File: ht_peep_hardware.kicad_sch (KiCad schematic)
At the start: 2 parts

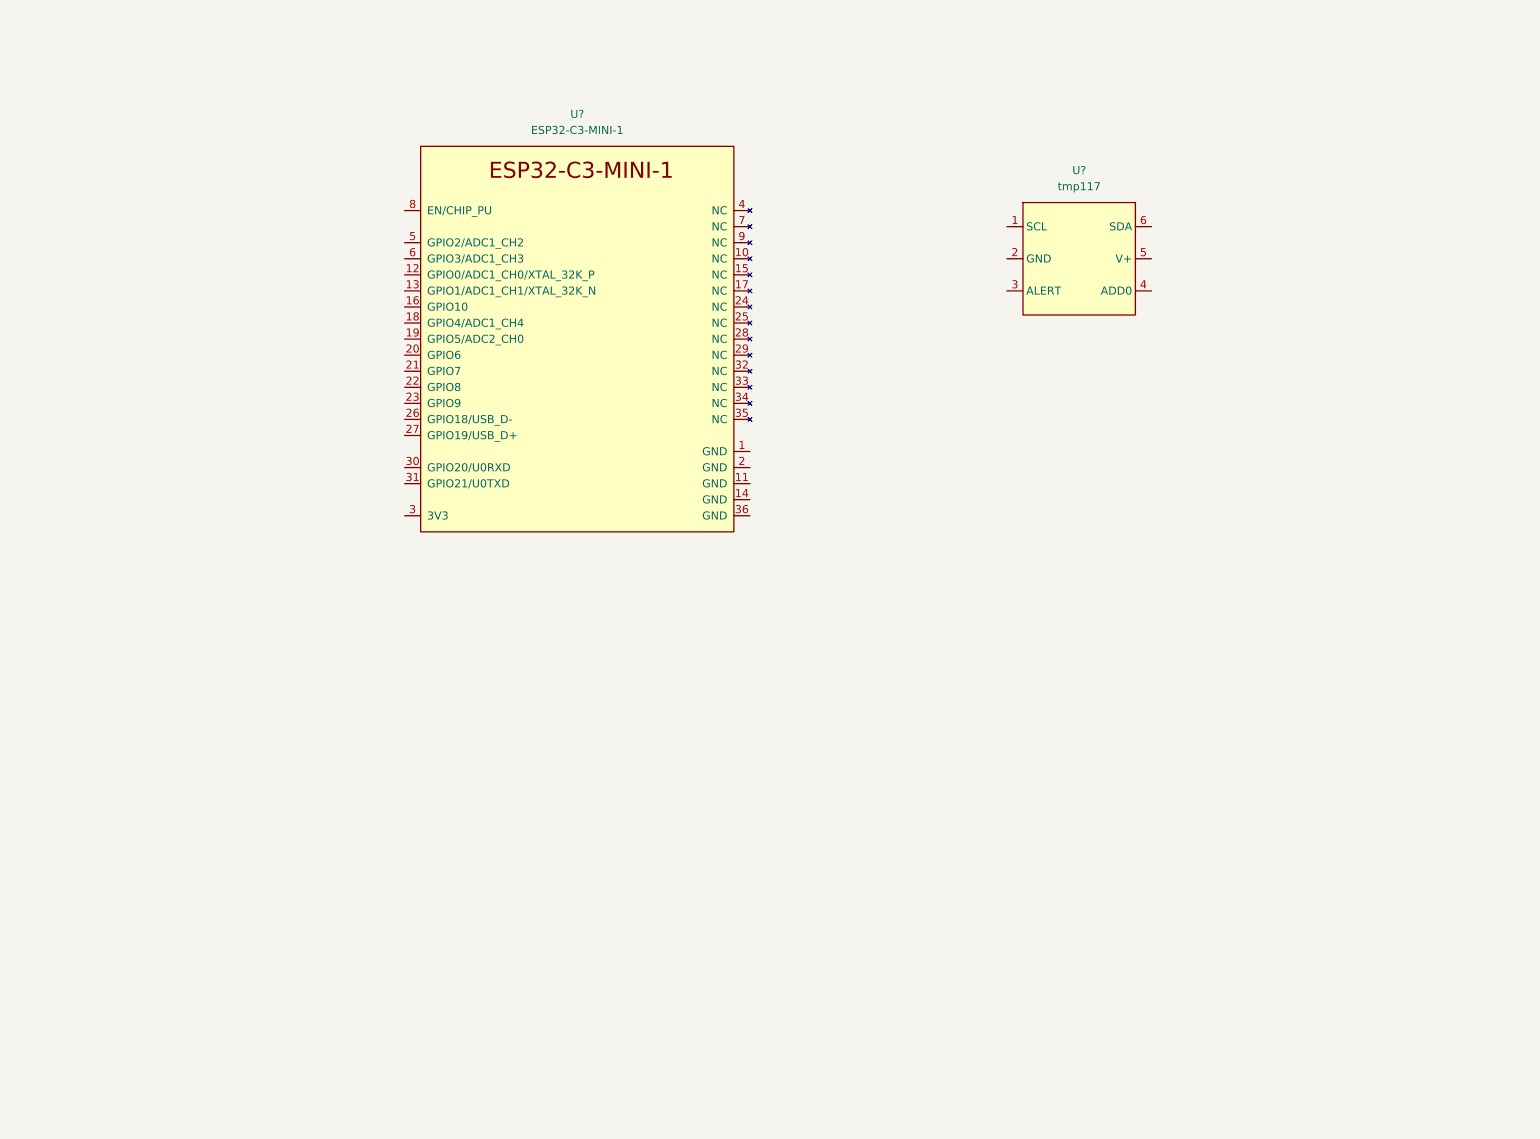
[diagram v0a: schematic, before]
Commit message: updated schematic w/ USB and C1 fix
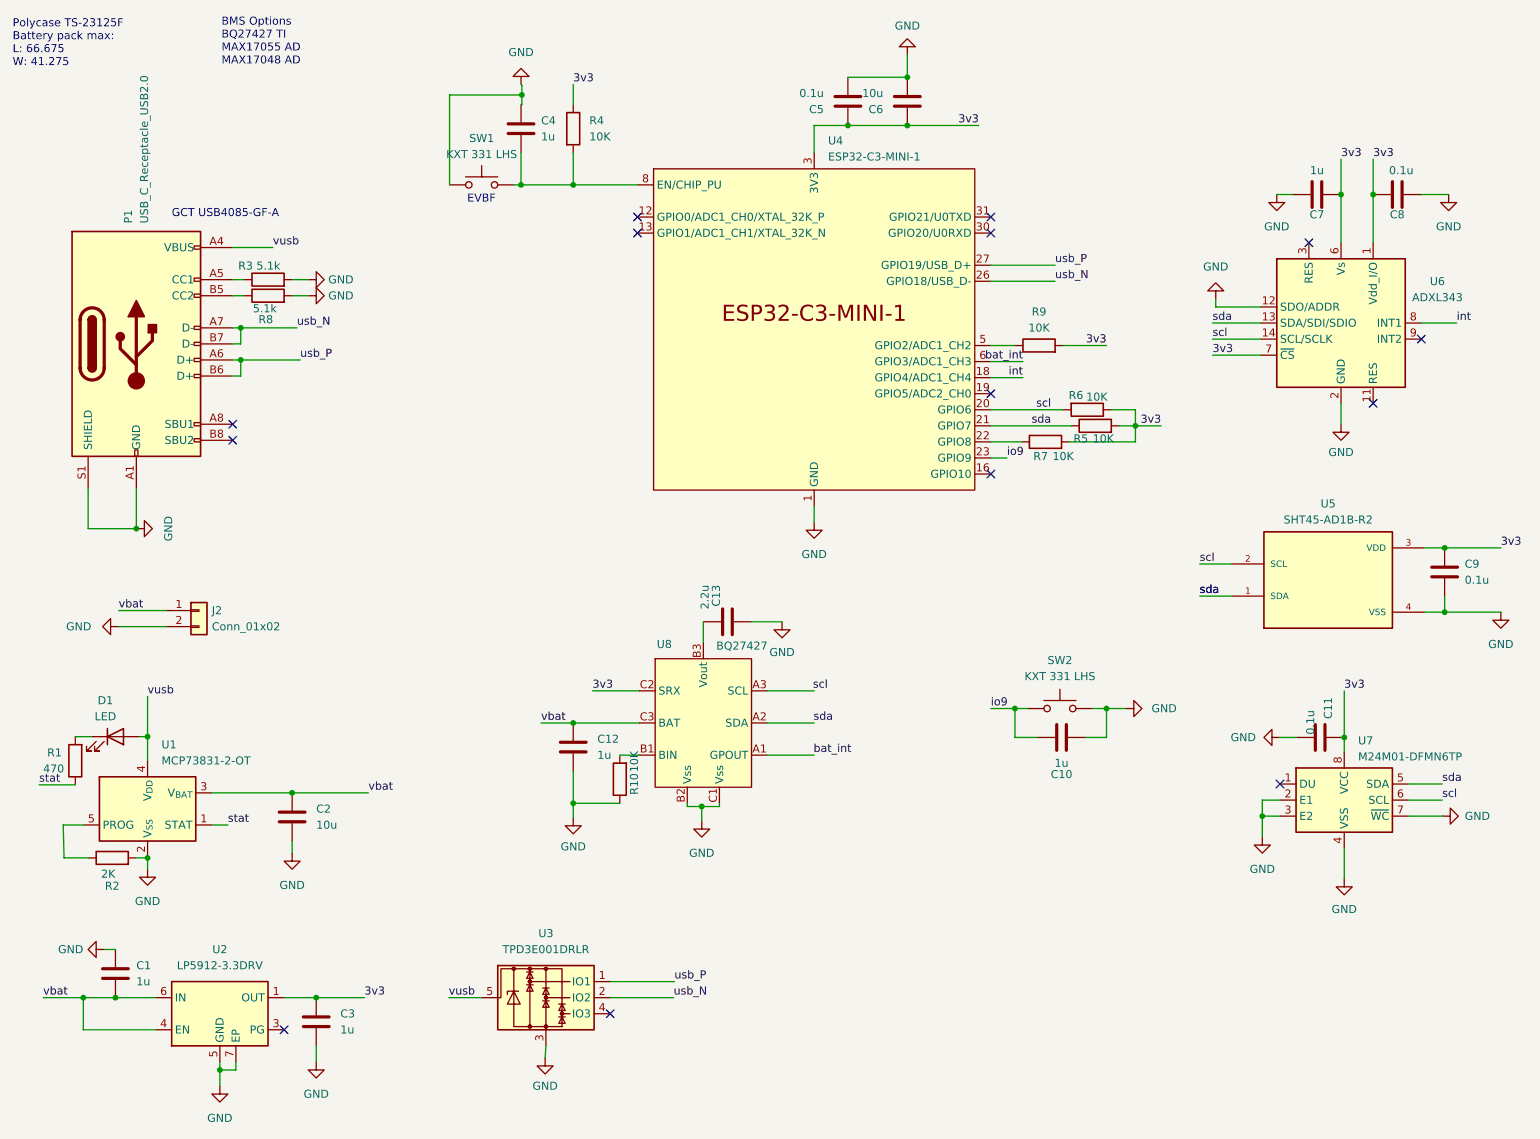
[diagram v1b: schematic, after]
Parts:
- removed U?: ESP32-C3-MINI-1, Espressif:ESP32-C3-MINI-1, symbol Espressif:ESP32-C3-MINI-1
- removed U?: tmp117, Package_SON:WSON-6-1EP_2x2mm_P0.65mm_EP1x1.6mm_ThermalVias, symbol ht_peep_hw:tmp117
- added C1, C10, C12, C3, C4, C7: 1u, Capacitor_SMD:C_0402_1005Metric, symbol Device:C
- added C11, C5, C8, C9: 0.1u, Capacitor_SMD:C_0402_1005Metric, symbol Device:C
- added C13: 2.2u, Capacitor_SMD:C_0402_1005Metric, symbol Device:C
- added C2, C6: 10u, Capacitor_SMD:C_0402_1005Metric, symbol Device:C
- added D1: LED, LED_SMD:LED_0402_1005Metric, symbol Device:LED
- added J2: Conn_01x02, Connector_JST:JST_ZE_S02B-ZESK-2D_1x02_P1.50mm_Horizontal, symbol Connector_Generic:Conn_01x02
- added P1: USB_C_Receptacle_USB2.0, Connector_USB:USB_C_Receptacle_GCT_USB4085, symbol Connector:USB_C_Receptacle_USB2.0
- added R1: 470, Resistor_SMD:R_0402_1005Metric, symbol Device:R
- added R10, R4, R5, R6, R7, R9: 10K, Resistor_SMD:R_0402_1005Metric, symbol Device:R
- added R2: 2K, Resistor_SMD:R_0402_1005Metric, symbol Device:R
- added R3, R8: 5.1k, Resistor_SMD:R_0402_1005Metric, symbol Device:R
- added SW1, SW2: KXT 331 LHS, Button_Switch_SMD:SW_SPST_CK_KXT3, symbol Switch:SW_Push
- added U1: MCP73831-2-OT, Package_TO_SOT_SMD:SOT-23-5, symbol Battery_Management:MCP73831-2-OT
- added U2: LP5912-3.3DRV, Package_SON:WSON-6-1EP_2x2mm_P0.65mm_EP1x1.6mm_ThermalVias, symbol Regulator_Linear:LP5912-3.3DRV
- added U3: TPD3E001DRLR, Package_TO_SOT_SMD:SOT-553, symbol Power_Protection:TPD3E001DRLR
- added U4: ESP32-C3-MINI-1, PCM_Espressif:ESP32-C3-MINI-1, symbol PCM_Espressif:ESP32-C3-MINI-1
- added U5: SHT45-AD1B-R2, sht45:SHT4X, symbol SHT45-AD1B-R2:SHT45-AD1B-R2
- added U6: ADXL343, Package_LGA:LGA-14_3x5mm_P0.8mm_LayoutBorder1x6y, symbol Sensor_Motion:ADXL343
- added U7: M24M01-DFMN6TP, Package_SO:SOIC-8_3.9x4.9mm_P1.27mm, symbol Memory_EEPROM:M24C02-RMN
- added U8: BQ27427, Package_BGA:Texas_DSBGA-9_1.4715x1.4715mm_Layout3x3_P0.5mm, symbol ht_peep_hw:BQ27427
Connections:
- new net: P1.B5 (CC2), R8.1
- new net: R7.1, U4.22 (GPIO8)
- new net: R9.1, U4.5 (GPIO2/ADC1_CH2)
- new net: C4.2, R4.2, SW1.2, U4.8 (EN/CHIP_PU)
- new net: P1.A5 (CC1), R3.1
- new net: D1.1 (K), R1.2
- new net: C13.1, U8.B3 (Vout)
- new net: R10.2, U8.B1 (BIN)
- new net: R2.1, U1.5 (PROG)
- new net 3v3: C11.2, C3.1, C5.1, C6.1, C7.1, C8.2, C9.1, R4.1, R5.2, R6.1, R7.2, R9.2, U2.1 (OUT), U4.3 (3V3), U5.3 (VDD), U6.1 (Vdd_I/O), U6.6 (Vs), U6.7 (~{CS}), U7.8 (VCC), U8.C2 (SRX)
- new net GND: C1.2, C10.1, C11.1, C12.2, C13.2, C2.2, C3.2, C4.1, C5.2, C6.2, C7.2, C8.1, C9.2, J2.2 (Pin_2), P1.A1 (GND), P1.A12 (GND), P1.B1 (GND), P1.B12 (GND), P1.S1 (SHIELD), R10.1, R2.2, R3.2, R8.2, SW1.1, SW2.2, U1.2 (V_{SS}), U2.5 (GND), U2.7 (EP), U3.3, U4.1 (GND), U4.11 (GND), U4.14 (GND), U4.2 (GND), U4.36 (GND), U4.37 (GND), U4.38 (GND), U4.39 (GND), U4.40 (GND), U4.41 (GND), U4.42 (GND), U4.43 (GND), U4.44 (GND), U4.45 (GND), U4.46 (GND), U4.47 (GND), U4.48 (GND), U4.49 (GND), U4.50 (GND), U4.51 (GND), U4.52 (GND), U4.53 (GND), U5.4 (VSS), U6.12 (SDO/ADDR), U6.2 (GND), U6.4 (GND), U6.5 (GND), U7.2 (E1), U7.3 (E2), U7.4 (VSS), U7.7 (~{WC}), U8.B2 (Vss), U8.C1 (Vss)
- new net bat_int: U4.6 (GPIO3/ADC1_CH3), U8.A1 (GPOUT)
- new net int: U4.18 (GPIO4/ADC1_CH4), U6.8 (INT1)
- new net io9: C10.2, SW2.1, U4.23 (GPIO9)
- new net scl: R6.2, U4.20 (GPIO6), U5.2 (SCL), U6.14 (SCL/SCLK), U7.6 (SCL), U8.A3 (SCL)
- new net sda: R5.1, U4.21 (GPIO7), U5.1 (SDA), U6.13 (SDA/SDI/SDIO), U7.5 (SDA), U8.A2 (SDA)
- new net stat: R1.1, U1.1 (STAT)
- new net usb_N: P1.A7 (D-), P1.B7 (D-), U3.2 (IO2), U4.26 (GPIO18/USB_D-)
- new net usb_P: P1.A6 (D+), P1.B6 (D+), U3.1 (IO1), U4.27 (GPIO19/USB_D+)
- new net vbat: C1.1, C12.1, C2.1, J2.1 (Pin_1), U1.3 (V_{BAT}), U2.4 (EN), U2.6 (IN), U8.C3 (BAT)
- new net vusb: D1.2 (A), P1.A4 (VBUS), P1.A9 (VBUS), P1.B4 (VBUS), P1.B9 (VBUS), U1.4 (V_{DD}), U3.5
- no-connect marks 0 -> 14
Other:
- note added: "BMS Options BQ27427 TI MAX17055 AD MAX17048 AD"
- note added: "EVBF"
- note added: "GCT USB4085-GF-A"
- note added: "Polycase TS-23125F Battery pack max: L: 66.675 W: 41.275"
